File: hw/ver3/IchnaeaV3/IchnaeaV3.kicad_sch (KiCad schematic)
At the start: 30 parts, among them J1 Terminal Block, J2 Terminal Block, U1 INA180A4, U19 INA180A4

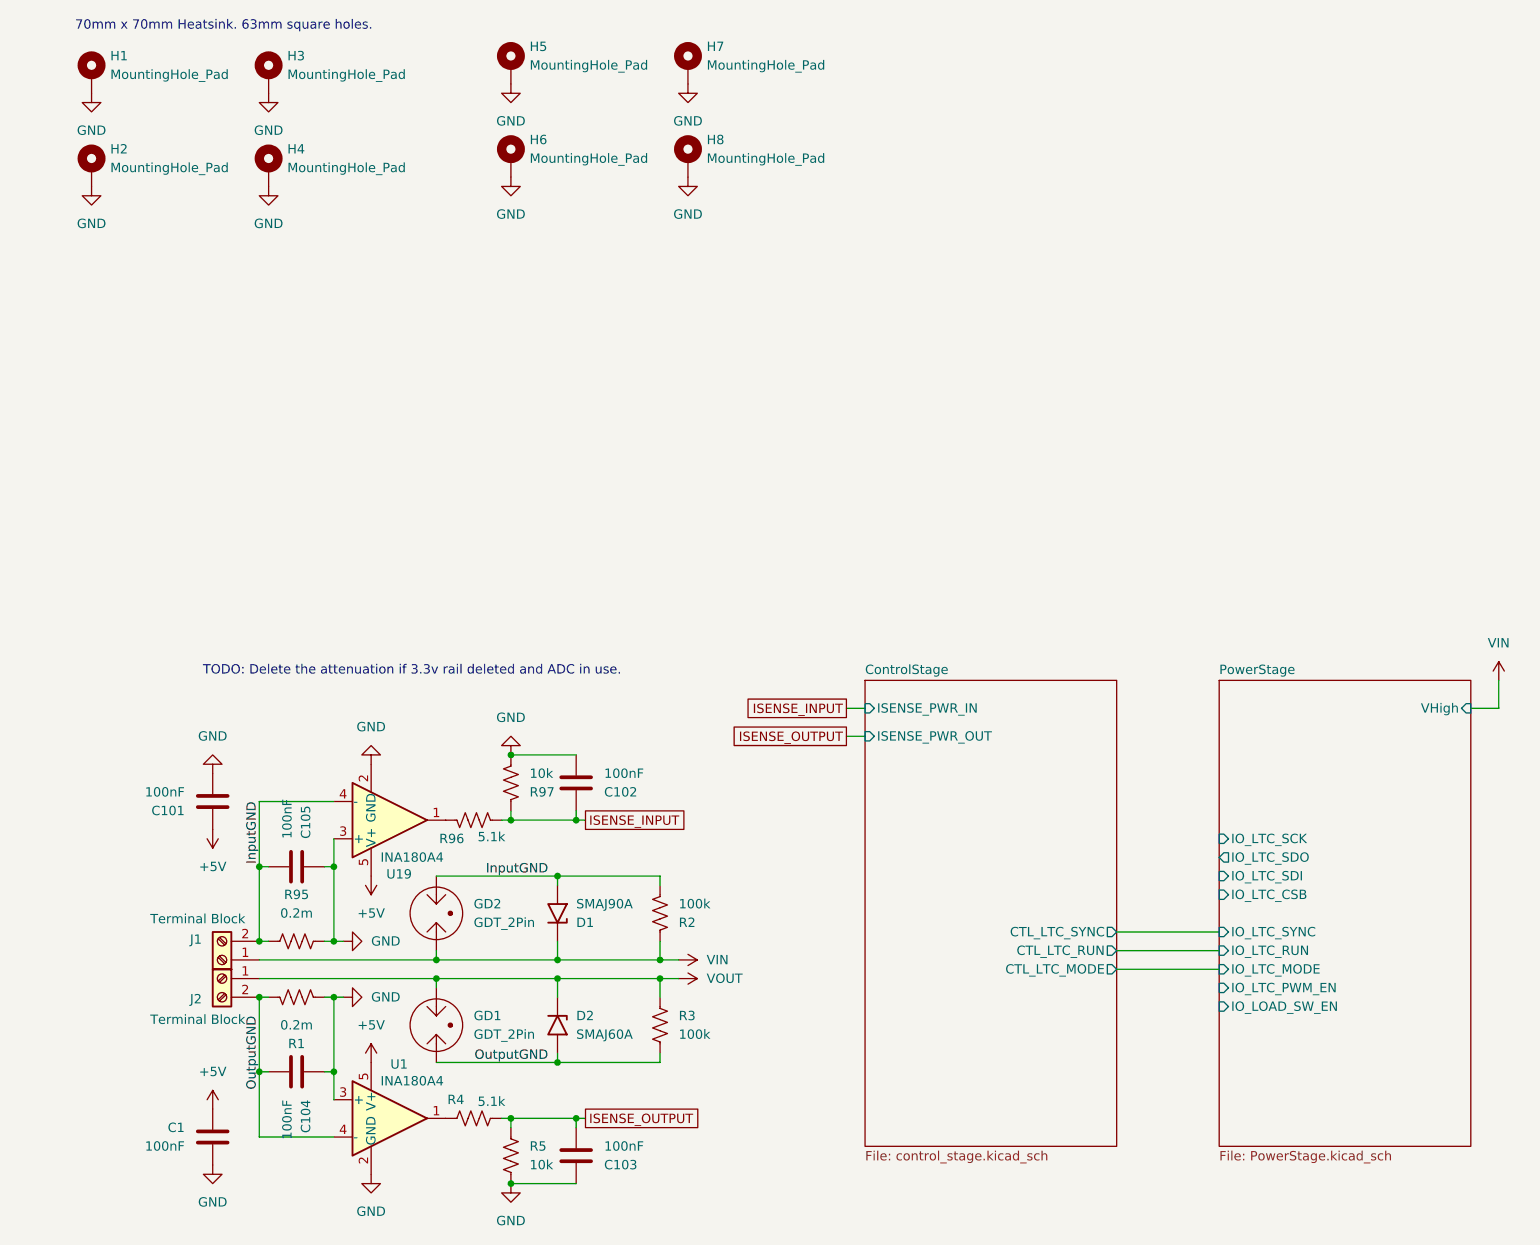
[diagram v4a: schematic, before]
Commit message: Improve more of the power stage layout
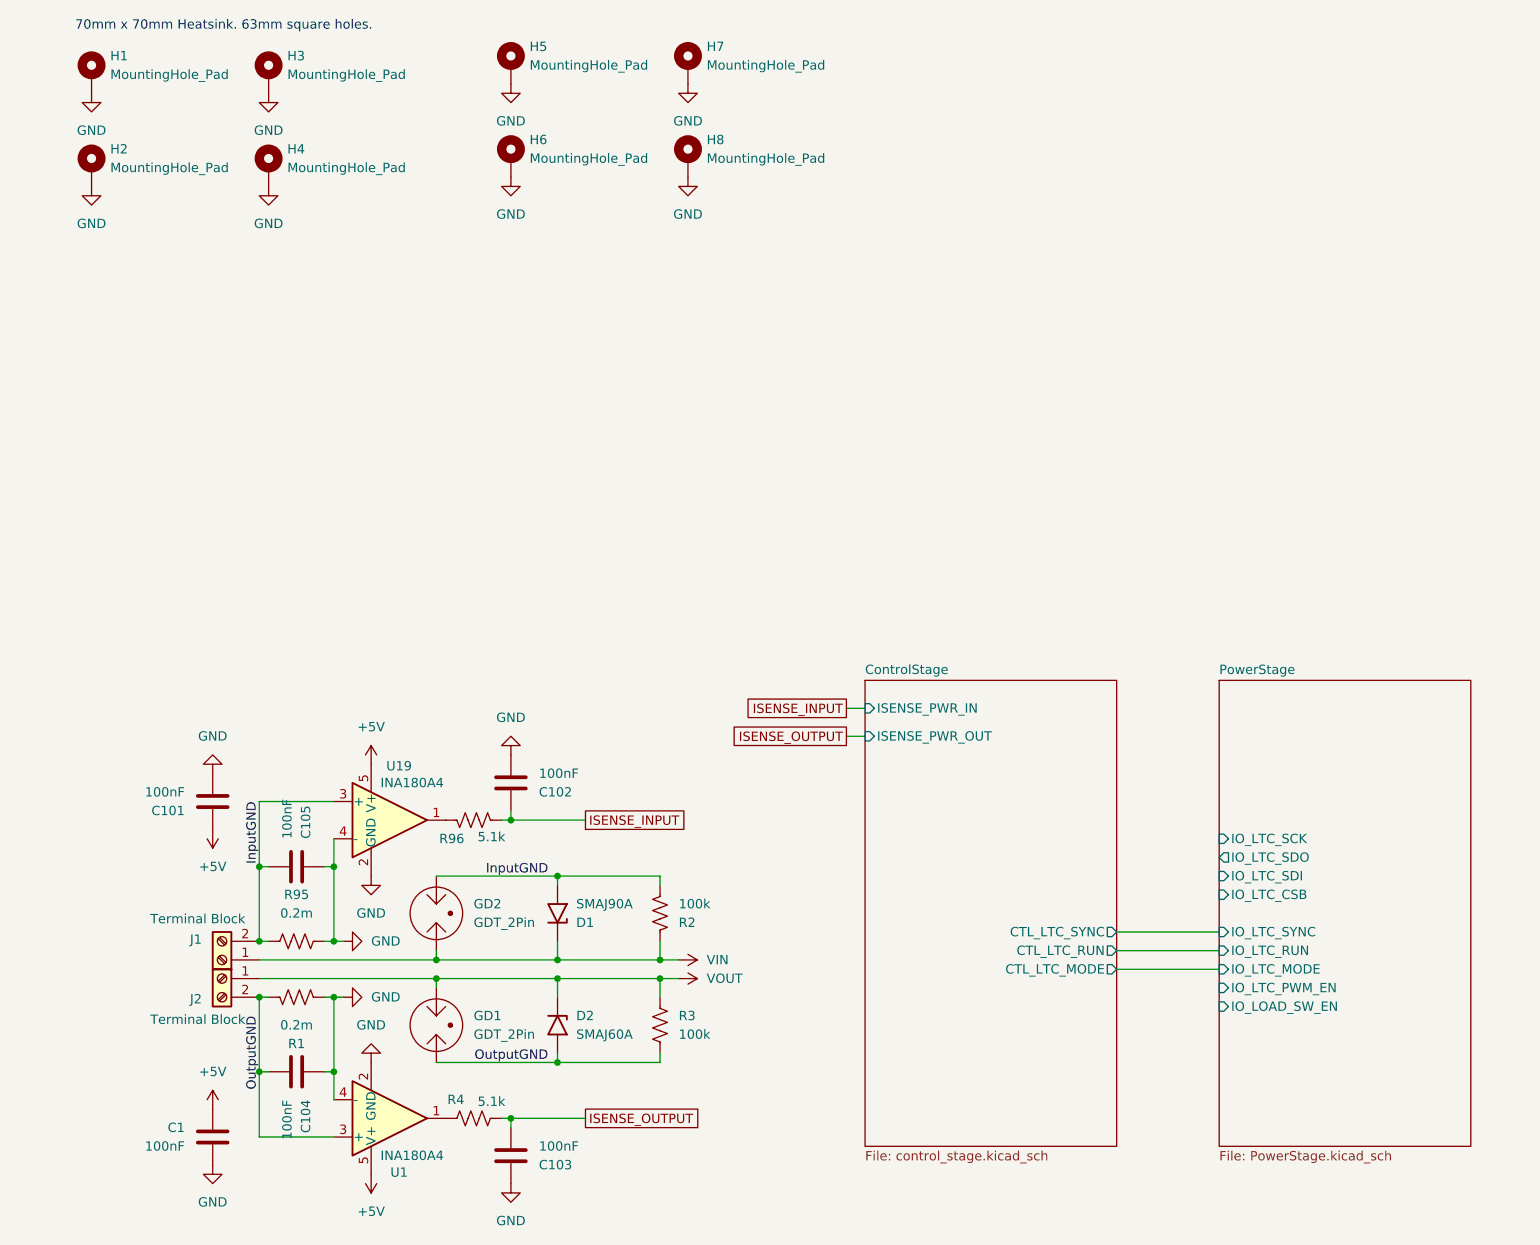
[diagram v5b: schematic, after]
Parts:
- removed R5, R97: 10k, Resistor_SMD:R_0603_1608Metric, symbol Device:R_US
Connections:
- net GND: now also U1.4 (-), U19.4 (-); no longer U1.3 (+), U19.3 (+)
- net InputGND: now also U19.3 (+); no longer U19.4 (-)
- net OutputGND: now also U1.3 (+); no longer U1.4 (-)
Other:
- sheet PowerStage ports: added none; removed VHigh
- note removed: "TODO: Delete the attenuation if 3.3v rail deleted and ADC in use."
- moved on the sheet: C102, C103
